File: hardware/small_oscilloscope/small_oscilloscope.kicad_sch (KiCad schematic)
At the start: 8 parts, among them J2 Parellel LCD, J5 Conn_01x16, J6 Conn_01x16, Q9 NTR5103NT1G, U2 FT800Q-T, Y1 12.0000M

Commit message: 250627 circuit
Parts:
- removed C4, C5: 20p, Capacitor_THT:C_Disc_D3.8mm_W2.6mm_P2.50mm, symbol Device:C
- removed J2: Parellel LCD, Connector_FFC-FPC:TE_4-1734839-0_1x40-1MP_P0.5mm_Horizontal, symbol LCD_interface:Conn_01x40_Pin
- removed Q9: NTR5103NT1G, symbol Transistor_FET:Q_NMOS_GSD
- removed U2: FT800Q-T, VQFN48_FT800_BRI, symbol FT800:FT800Q-T
- removed Y1: 12.0000M, Crystal:Crystal_HC49-4H_Vertical, symbol Device:Crystal
- added R1: 10k, Resistor_SMD:R_0402_1005Metric_Pad0.72x0.64mm_HandSolder, symbol Device:R
- added U1: CH423S, Package_SO:SOP-28_8.4x18.16mm_P1.27mm, symbol giho_user:CH423s
- renumbered J5 to J1, J6 to J2
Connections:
- net +3.3V: now also U1.25 (VCC)
- net +5V: now also R1.1
- net GND: now also U1.11 (GND)
- net Power/BACKLIGHT: now also R1.2
- net TRIG0: now reaches J2.10 (17)
- net TRIG1: now reaches J2.11 (16)
- net MOSI: now reaches J2.2 (23)
- net SCL: now reaches J2.3 (22)
- net SCL: now also U1.9 (SCL)
- net SDA: now reaches J2.6 (21)
- net SDA: now also U1.10 (SDA)
- net MISO: now reaches J2.7 (19)
- net SCK: now reaches J2.8 (18)
- net SS: now reaches J2.9 (5)
- net RE1B: now reaches J1.10 (27)
- net RE1A: now reaches J1.11 (14)
- net RE0B: now reaches J1.12
- net RE0A: now reaches J1.13
- net ADC0: now reaches J1.3 (Vp)
- net ADC1: now reaches J1.4 (Vn)
- net TRIG: now reaches J1.8 (25)
- new net LCD UI/LED0: U1.19 (OC12)
- new net LCD UI/LED1: U1.20 (OC13)
- new net LCD UI/LEDRE0: U1.21 (OC14)
- new net LCD UI/LEDRE1: U1.22 (OC15)
- new net LCD UI/RE0P: U1.23 (IO0)
- new net LCD UI/RE1P: U1.24 (IO1)
- new net LCD UI/SW0: U1.26 (IO2)
- new net LCD UI/SW1: U1.27 (IO3)
- new net LCD UI/SW2: U1.28 (IO4)
- new net LCD UI/SW3: U1.1 (IO5)
- new net Q1: U1.4 (OC0)
- new net Q10: U1.16 (OC9)
- new net Q11: U1.17 (OC10)
- new net Q12: U1.18 (OC11)
- new net Q2: U1.5 (OC1)
- new net Q3: U1.6 (OC2)
- new net Q4: U1.7 (OC3)
- new net Q5: U1.8 (OC4)
- new net Q6: U1.12 (OC5)
- new net Q7: U1.13 (OC6)
- new net Q8: U1.14 (OC7)
- new net Q9: U1.15 (OC8)
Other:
- removed sheet Audio
- added sheet LCD (lcd.kicad_sch)
- sheet LCD UI ports: added 3V3, GND, LED0, LED1, LEDRE0, LEDRE1, RE0A, RE0B, RE0P, RE1A, RE1B, RE1P, SW0, SW1, SW2, SW3; removed none
- sheet Power ports: added 5V; removed none
- moved on the sheet: J1, J2

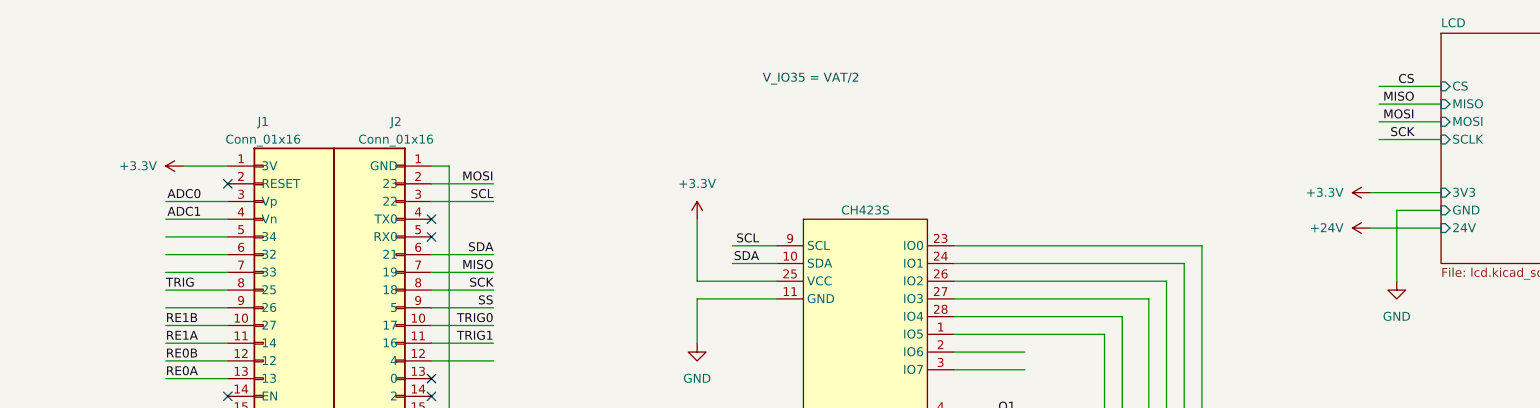
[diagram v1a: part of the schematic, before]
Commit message: feat: 오실로스코프 회로 설계 업데이트
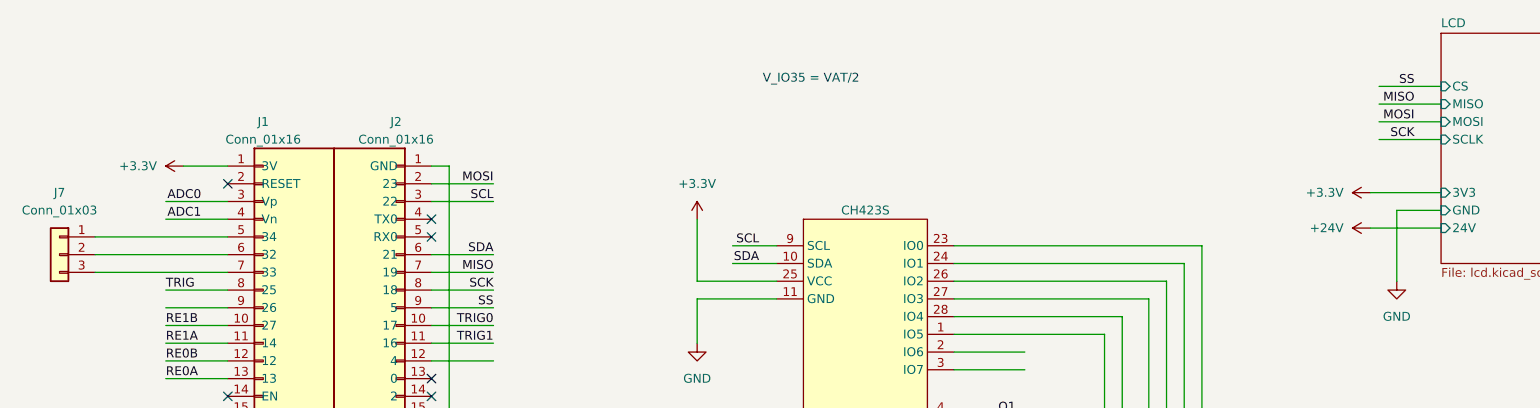
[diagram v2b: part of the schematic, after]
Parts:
- added J7: Conn_01x03, Connector_PinHeader_2.54mm:PinHeader_1x03_P2.54mm_Vertical, symbol Connector_Generic:Conn_01x03
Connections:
- net at J1.5 (34): now also J7.1 (Pin_1)
- net at J1.6 (32): now also J7.2 (Pin_2)
- net at J1.7 (33): now also J7.3 (Pin_3)
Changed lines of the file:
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@@
 	(wire
 		(pts
-			(xy 55.88 64.77) (xy 64.77 64.77)
-		)
-		(stroke
-			(width 0)
-			(type default)
-		)
-	)
-	(wire
-		(pts
-			(xy 55.88 59.69) (xy 64.77 59.69)
+			(xy 45.72 64.77) (xy 64.77 64.77)
+		)
+		(stroke
+			(width 0)
+			(type default)
+		)
+	)
+	(wire
+		(pts
+			(xy 45.72 59.69) (xy 64.77 59.69)
 		)
 		(stroke
@@
 	(wire
 		(pts
-			(xy 55.88 62.23) (xy 64.77 62.23)
+			(xy 45.72 62.23) (xy 64.77 62.23)
 		)
 		(stroke
@@
 		)
 	)
-	(label "CS"
+	(label "SS"
 		(at 234.95 38.1 180)
 		(effects
@@
 		)
 	)
+	(symbol
+		(lib_id "Connector_Generic:Conn_01x03")
+		(at 40.64 62.23 0)
+		(mirror y)
+		(unit 1)
+		(exclude_from_sim no)
+		(in_bom yes)
+		(on_board yes)
+		(dnp no)
+		(fields_autoplaced yes)
+		(property "Reference" "J7"
+			(at 40.64 53.34 0)
+			(effects
+				(font
+					(size 1.27 1.27)
+				)
+			)
+		)
+		(property "Value" "Conn_01x03"
+			(at 40.64 55.88 0)
+			(effects
+				(font
+					(size 1.27 1.27)
+				)
+			)
+		)
+		(property "Footprint" "Connector_PinHeader_2.54mm:PinHeader_1x03_P2.54mm_Vertical"
+			(at 40.64 62.23 0)
+			(effects
+				(font
+					(size 1.27 1.27)
+				)
+				(hide yes)
+			)
+		)
+		(property "Datasheet" "~"
+			(at 40.64 62.23 0)
+			(effects
+				(font
+					(size 1.27 1.27)
+				)
+				(hide yes)
+			)
+		)
+		(property "Description" "Generic connector, single row, 01x03, script generated (kicad-library-utils/schlib/autogen/connector/)"
+			(at 40.64 62.23 0)
+			(effects
+				(font
+					(size 1.27 1.27)
+				)
+				(hide yes)
+			)
+		)
+		(pin "3"
+		)
+		(pin "1"
+		)
+		(pin "2"
+		)
+		(instances
+			(project ""
+				(path "/722ad30e-a672-4959-92bf-662e54054c44"
+					(reference "J7")
+					(unit 1)
+				)
+			)
+		)
+	)

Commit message: oscilliscope first success
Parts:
- removed J1, J2: Conn_01x16, Connector_PinSocket_2.54mm:PinSocket_1x16_P2.54mm_Vertical, symbol Connector_Generic:Conn_01x16
- removed J7: Conn_01x03, Connector_PinHeader_2.54mm:PinHeader_1x03_P2.54mm_Vertical, symbol Connector_Generic:Conn_01x03
- added AE1: Antenna_Chip, Inductor_SMD:L_1206_3216Metric_Pad1.22x1.90mm_HandSolder, symbol Device:Antenna_Chip
- added C1: 10u, Capacitor_SMD:CP_Elec_5x5.3, symbol Device:C_Polarized
- added C2: 0.1u, Capacitor_SMD:C_0402_1005Metric_Pad0.74x0.62mm_HandSolder, symbol Device:C
- added D1: 1N5225B, Diode_THT:D_A-405_P7.62mm_Horizontal, symbol Diode:1N47xxA
- added J1: SIGNAL, Connector_PinSocket_2.54mm:PinSocket_1x02_P2.54mm_Vertical, symbol Connector_Generic:Conn_01x02
- added Q1, Q2: 2SC4671, Package_TO_SOT_SMD:SOT-523, symbol Transistor_BJT:2SC4213
- added R10, R11, R2, R3, R4, R5, R6, R7, R8, R9: 10k, Resistor_SMD:R_0402_1005Metric_Pad0.72x0.64mm_HandSolder, symbol Device:R
- added R12, R14, R15, R17, R18, R21, R22: 10K, Resistor_SMD:R_0402_1005Metric_Pad0.72x0.64mm_HandSolder, symbol Device:R
- added R13: 100, Resistor_SMD:R_0603_1608Metric_Pad0.98x0.95mm_HandSolder, symbol Device:R
- added R16: 4K7, Resistor_SMD:R_0402_1005Metric_Pad0.72x0.64mm_HandSolder, symbol Device:R
- added R19: 3K, Resistor_SMD:R_0402_1005Metric_Pad0.72x0.64mm_HandSolder, symbol Device:R
- added R20: 820R, Resistor_SMD:R_0402_1005Metric_Pad0.72x0.64mm_HandSolder, symbol Device:R
- added R23, R24: 1k, Resistor_SMD:R_0603_1608Metric_Pad0.98x0.95mm_HandSolder, symbol Device:R
- added U2: ESP32-PICO-D4, Package_DFN_QFN:QFN-48-1EP_7x7mm_P0.5mm_EP5.3x5.3mm, symbol MCU_Espressif:ESP32-PICO-D4
- R1: now left out of the parts list
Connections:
- net Power/BACKLIGHT is gone; now on net SCL: R1.2
- net +3.3V: now also R1.1, C1.1, C2.1, R17.1, R2.1, R3.1, R7.1, R8.1, R9.1, U2.1 (VDDA), U2.19 (VDD3P3_RTC), U2.3 (VDDA3P3), U2.37 (VDD3P3_CPU), U2.4 (VDDA3P3), U2.43 (VDDA), U2.46 (VDDA)
- net +5V: now also R13.1, R15.1; no longer R1.1
- net ADC0: now also U2.10 (IO34)
- net ADC1: now also U2.24 (IO4)
- net GND: now also C1.2, C2.2, D1.2 (A), Q1.2 (E), Q2.2 (E), R18.2, R19.2, R20.2, R21.2, R22.2, R4.2, U2.49 (GND)
- net MISO: now also U2.38 (IO19)
- net MOSI: now also U2.36 (IO23)
- net RE0A: now also U2.21 (IO15)
- net RE0B: now also U2.17 (IO14)
- net RE1A: now also U2.20 (IO13)
- net RE1B: now also U2.18 (IO12)
- net SCK: now also U2.35 (IO18)
- net SCL: now also U2.42 (IO21)
- net SDA: now also R2.2, U2.39 (IO22)
- net SS: now also R7.2, U2.34 (IO5)
- net TRIG: now also U2.14 (IO25)
- net TRIG0: now also R6.2, U2.28 (SD2/IO9)
- net TRIG1: now also R5.2, U2.29 (SD3/IO10)
- net ~{STDBY}: now reaches U1.2 (IO6)
- net ~{STDBY}: now also Q2.3 (C), R9.2
- net ~{CHRG}: now reaches U1.3 (IO7)
- net ~{CHRG}: now also Q1.3 (C), R8.2
- net Q2 renamed BACKLIGHT
- net Q8: no longer names the net of U1.14 (OC7)
- new net: Q1.1 (B), R10.2
- new net: D1.1 (K), R12.1, R13.2
- new net: Q2.1 (B), R11.2
- new net +12V: R16.1
- new net ANT50R: AE1.1 (FEED), U2.2 (LNA_IN)
- new net EN: R3.2, U2.9 (EN)
- new net IO0: U2.23 (IO0)
- new net IO2: R4.1, U2.22 (IO2)
- new net Power/~{CHRG}: R10.1
- new net Power/~{STDBY}: R11.1
- new net RXD: R23.2, U2.40 (U0RXD/IO3)
- new net TESTPIN: J1.1 (Pin_1), J1.2 (Pin_2), U2.15 (IO26)
- new net TXD: R24.2, U2.41 (U0TXD/IO1)
- new net USB Serial/RXD: R24.1
- new net USB Serial/TXD: R23.1
- new net VDD_SDIO: R5.1, R6.1, U2.26 (VDD_SDIO)
- new net VREF1.5V: R12.2, R22.1, U2.8 (SENSOR_VN)
- new net VREF12V: R16.2, R20.1, U2.7 (SENSOR_CAPN)
- new net VREF3V3: R17.2, R21.1, U2.11 (IO35)
- new net VREF5V: R15.2, R19.1, U2.6 (SENSOR_CAPP)
- new net VREFBAT: R14.2, R18.1, U2.5 (SENSOR_VP)
- new net Vbat: R14.1
- new net ~{INT}: U2.16 (IO27)
- no-connect marks 7 -> 6
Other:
- added sheet USB Serial (usb_serial.kicad_sch)
- sheet Analog ports: added +5V; removed Q2, Q8
- sheet LCD ports: added ~{INT}, ~{PD}; removed none
- sheet Power ports: added -12V, 12V, VBAT, Vusb, ~{CHRG}, ~{STDBY}; removed -V
- note added: "IO15=1 : U0TXD Printing Control Enable IO12=0 : VDD_SDIO=3.3 else 1.8 IO5 =1 : SDIO Slave rising edge output IO15=1 : SDIO Slave rising edge sampling"
- note added: "Vbat : 2.7V~4.2V +5V : 5V +12V : 12V +3V3 : 3.3V Vbat : 10:10 : 1/2 : 1.35V~2.10V +5V : 3:10 : 1/4.333 : 1.15V +12V : 0.820:4.7 : 1/6.732 : 1.78V +3V3 : 10:10 : 1/2 : 1.65V"
